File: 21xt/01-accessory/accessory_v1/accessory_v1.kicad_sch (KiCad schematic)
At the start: 31 parts, among them IC1 LT6658AHMSE-2.5#PBF, IC2 LT6658AHMSE-5#PBF, IC3 REF5025AIDR, IC7 REF5050IDR, J1 Conn_01x04

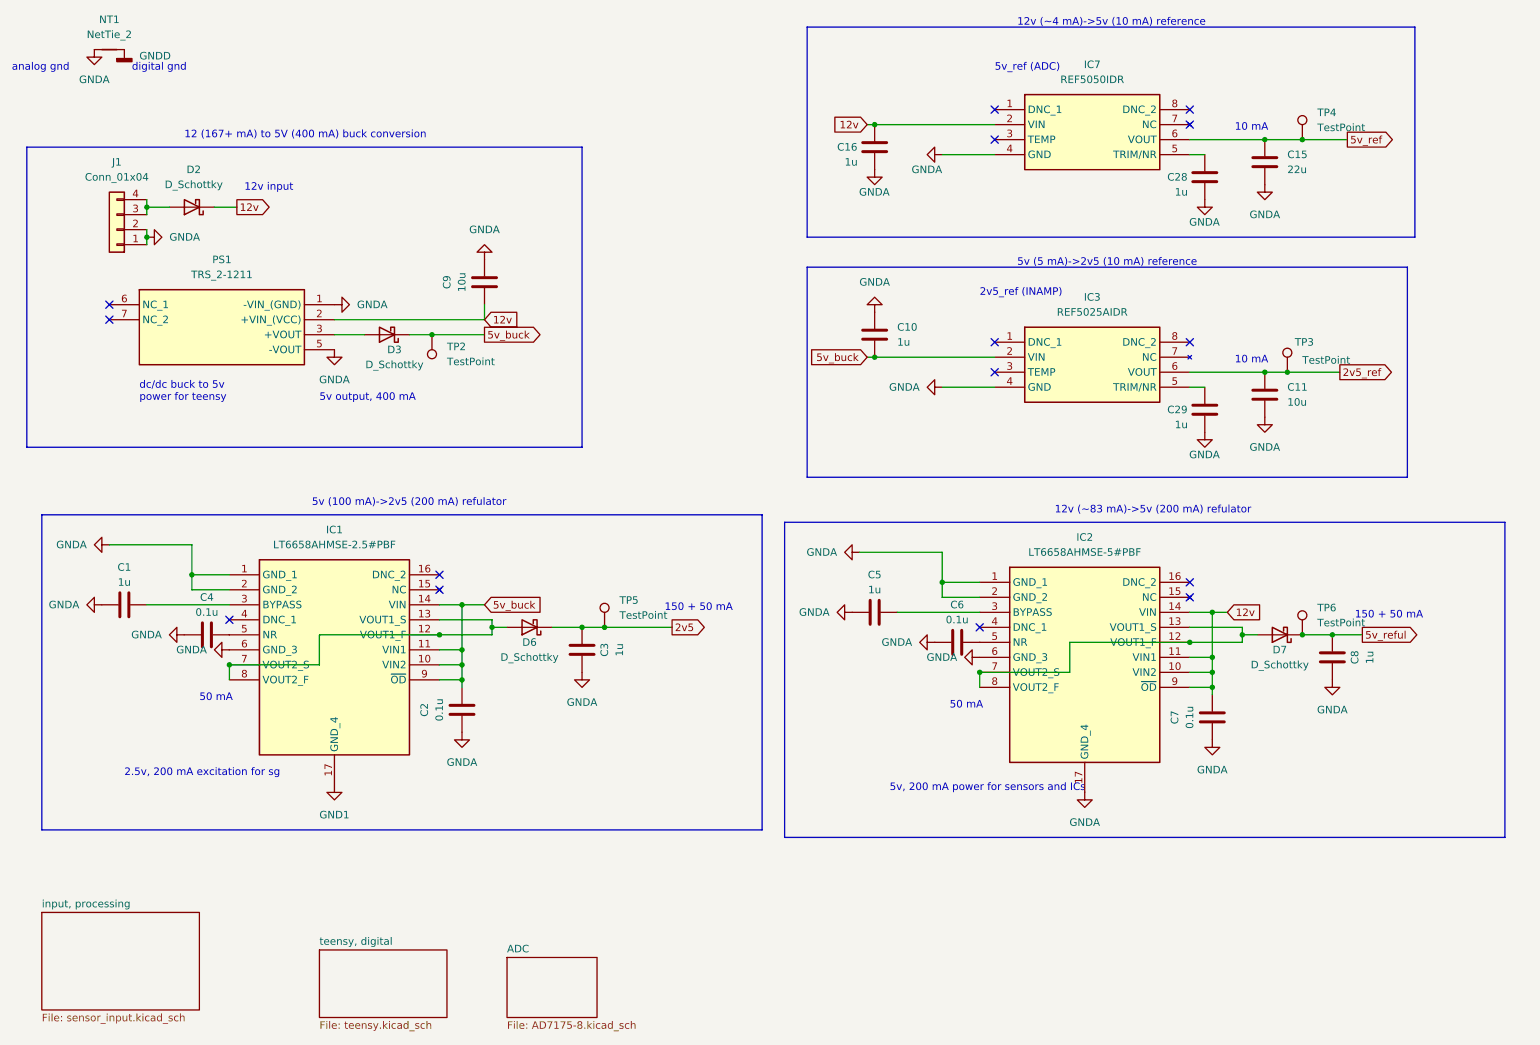
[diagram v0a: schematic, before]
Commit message: Added all accessory Rev1 3d models, added 3d models to 3d model folder and updated footprints
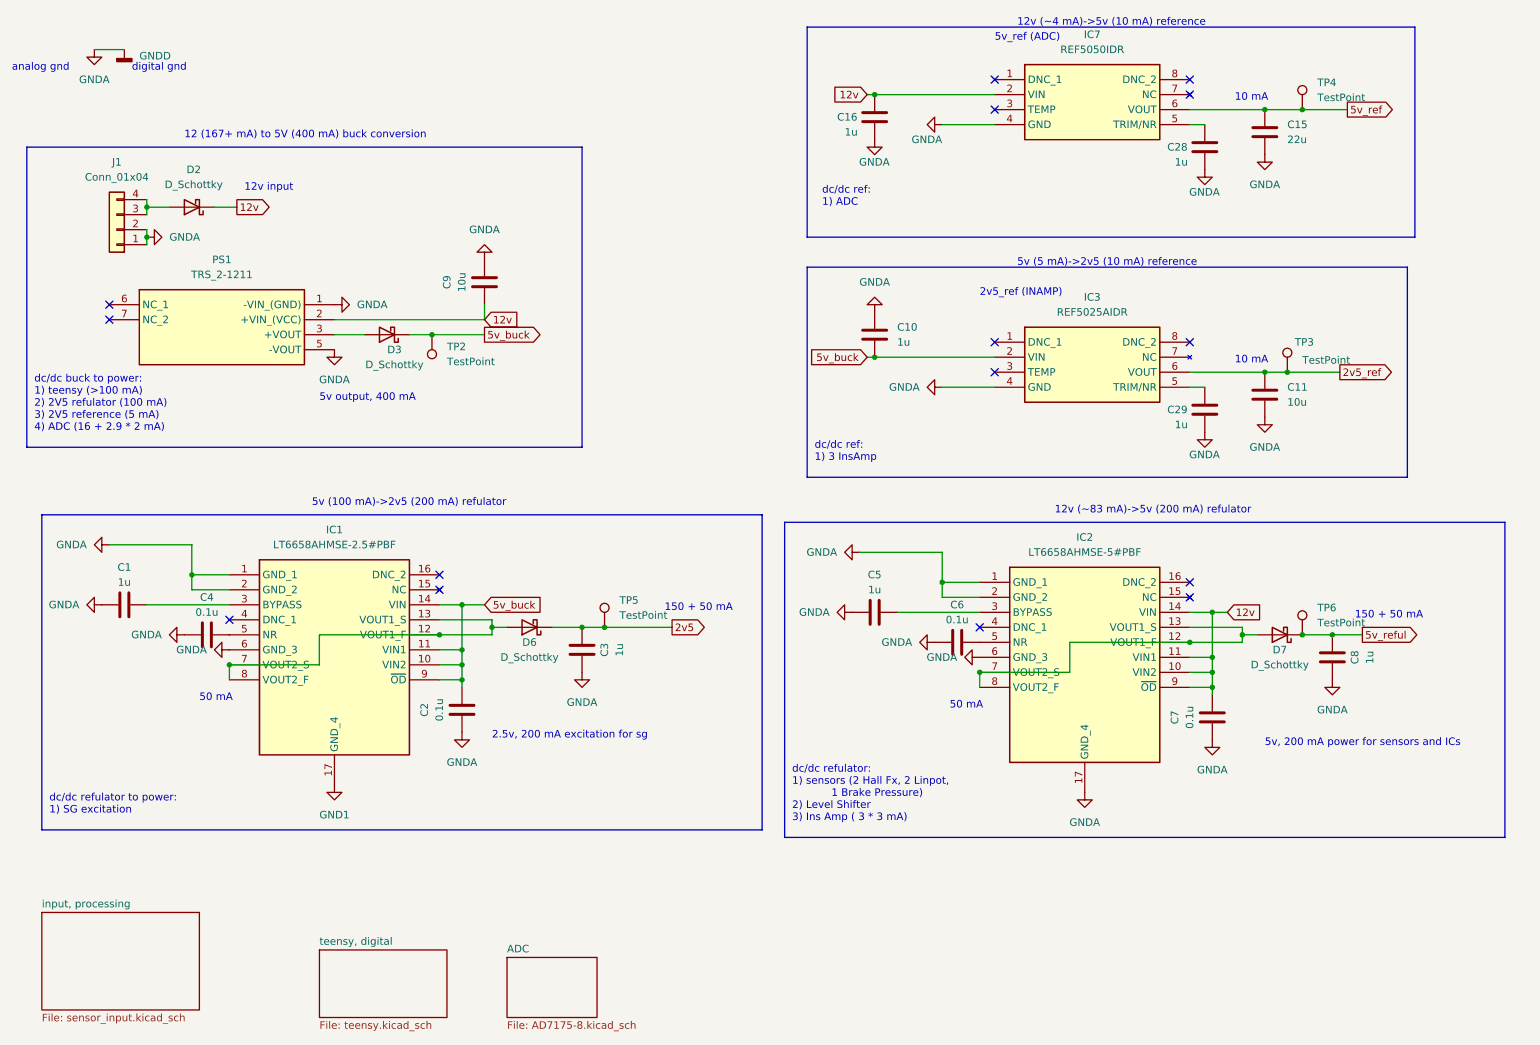
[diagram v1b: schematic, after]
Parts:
- removed NT1: NetTie_2, symbol Device:NetTie_2
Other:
- note added: "dc/dc buck to power: 1) teensy (>100 mA) 2) 2V5 refulator (100 mA) 3) 2V5 reference (5 mA) 4) ADC (16 + 2.9 * 2 mA)"
- note added: "dc/dc ref: 1) 3 InsAmp"
- note added: "dc/dc ref: 1) ADC"
- note added: "dc/dc refulator to power: 1) SG excitation"
- note added: "dc/dc refulator: 1) sensors (2 Hall Fx, 2 Linpot, 1 Brake Pressure) 2) Level Shifter 3) Ins Amp ( 3 * 3 mA)"
- note removed: "dc/dc buck to 5v power for teensy"
- moved on the sheet: C15, C16, C28, IC7, TP4

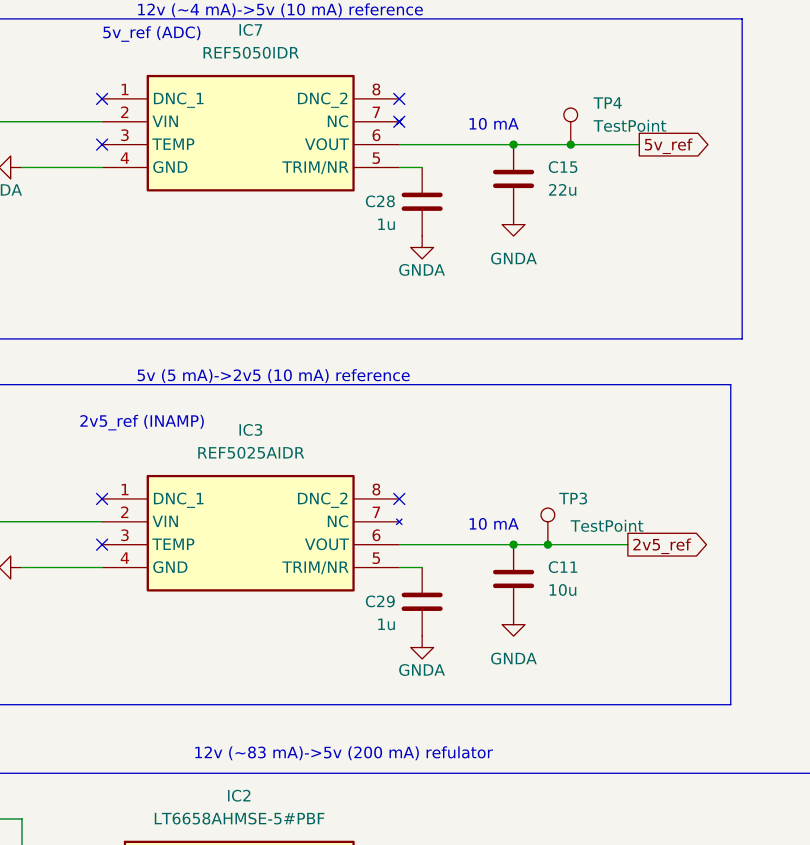
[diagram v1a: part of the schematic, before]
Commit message: Accessory V2 schematic almost done, only missing TVS diodes and checking
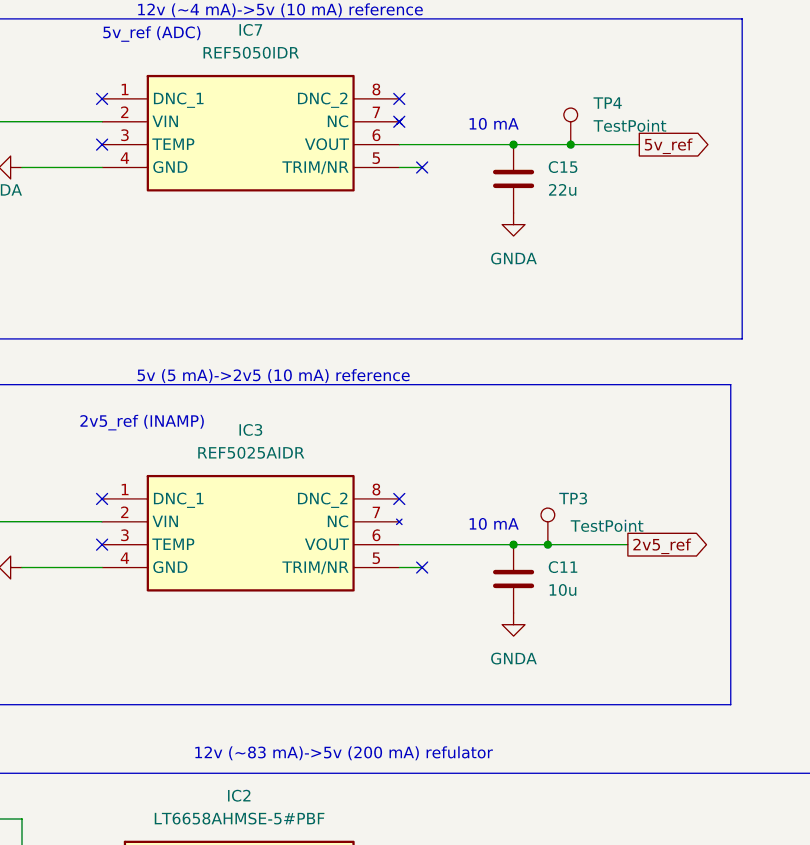
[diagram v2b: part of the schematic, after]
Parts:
- removed C28, C29: 1u, Capacitor_SMD:C_0603_1608Metric, symbol Device:C
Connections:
- no-connect marks 15 -> 17
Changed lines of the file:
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@@
   (no_connect (at 184.15 76.2))
   (no_connect (at 184.15 26.67))
+  (no_connect (at 219.71 78.74))
   (no_connect (at 217.17 29.21))
   (no_connect (at 34.29 64.77))
   (no_connect (at 217.17 71.12))
   (no_connect (at 90.17 110.49))
+  (no_connect (at 219.71 34.29))
   (no_connect (at 217.17 26.67))
   (no_connect (at 217.17 114.3))
@@
     )
   )
-  (symbol (lib_id "power:GNDA") (at 219.71 86.36 0) (unit 1)
-    (in_bom yes) (on_board yes) (dnp no)
-    (property "Reference" "#PWR064" (at 219.71 92.71 0)
-      (effects (font (size 1.27 1.27)) hide)
-    )
-    (property "Value" "GNDA" (at 222.25 90.17 0)
-      (effects (font (size 1.27 1.27)) (justify right))
-    )
-    (property "Footprint" "" (at 219.71 86.36 0)
-      (effects (font (size 1.27 1.27)) hide)
-    )
-    (property "Datasheet" "" (at 219.71 86.36 0)
-      (effects (font (size 1.27 1.27)) hide)
-    )
-    (pin "1")
-    (instances
-      (project "accessory_v1"
-        (path "/5dacc41e-ffff-47d3-9300-200c6018c603"
-          (reference "#PWR064") (unit 1)
-        )
-      )
-    )
-  )
   (symbol (lib_id "power:GNDA") (at 114.3 127 0) (unit 1)
     (in_bom yes) (on_board yes) (dnp no) (fields_autoplaced)
@@
     )
   )
-  (symbol (lib_id "power:GNDA") (at 219.71 41.91 0) (unit 1)
-    (in_bom yes) (on_board yes) (dnp no)
-    (property "Reference" "#PWR063" (at 219.71 48.26 0)
-      (effects (font (size 1.27 1.27)) hide)
-    )
-    (property "Value" "GNDA" (at 222.25 45.72 0)
-      (effects (font (size 1.27 1.27)) (justify right))
-    )
-    (property "Footprint" "" (at 219.71 41.91 0)
-      (effects (font (size 1.27 1.27)) hide)
-    )
-    (property "Datasheet" "" (at 219.71 41.91 0)
-      (effects (font (size 1.27 1.27)) hide)
-    )
-    (pin "1")
-    (instances
-      (project "accessory_v1"
-        (path "/5dacc41e-ffff-47d3-9300-200c6018c603"
-          (reference "#PWR063") (unit 1)
-        )
-      )
-    )
-  )
   (symbol (lib_id "power:GNDA") (at 220.98 138.43 0) (unit 1)
     (in_bom yes) (on_board yes) (dnp no) (fields_autoplaced)
@@
         )
       )
-    )
-  )
-  (symbol (lib_id "Device:C") (at 219.71 82.55 0) (unit 1)
-    (in_bom yes) (on_board yes) (dnp no)
-    (property "Reference" "C29" (at 213.36 82.55 0)
-      (effects (font (size 1.27 1.27)) (justify left))
-    )
-    (property "Value" "1u" (at 214.63 85.09 0)
-      (effects (font (size 1.27 1.27)) (justify left))
-    )
-    (property "Footprint" "Capacitor_SMD:C_0603_1608Metric" (at 220.6752 86.36 0)
-      (effects (font (size 1.27 1.27)) hide)
-    )
-    (property "Datasheet" "~" (at 219.71 82.55 0)
-      (effects (font (size 1.27 1.27)) hide)
-    )
-    (pin "2")
-    (pin "1")
-    (instances
-      (project "accessory_v1"
-        (path "/5dacc41e-ffff-47d3-9300-200c6018c603"
-          (reference "C29") (unit 1)
-        )
-      )
-    )
-  )
-  (symbol (lib_id "Device:C") (at 219.71 38.1 0) (unit 1)
-    (in_bom yes) (on_board yes) (dnp no)
-    (property "Reference" "C28" (at 213.36 38.1 0)
-      (effects (font (size 1.27 1.27)) (justify left))
-    )
-    (property "Value" "1u" (at 214.63 40.64 0)
-      (effects (font (size 1.27 1.27)) (justify left))
-    )
-    (property "Footprint" "Capacitor_SMD:C_0603_1608Metric" (at 220.6752 41.91 0)
-      (effects (font (size 1.27 1.27)) hide)
-    )
-    (property "Datasheet" "~" (at 219.71 38.1 0)
-      (effects (font (size 1.27 1.27)) hide)
-    )
-    (pin "2")
-    (pin "1")
-    (instances
-      (project "accessory_v1"
-        (path "/5dacc41e-ffff-47d3-9300-200c6018c603"
-          (reference "C28") (unit 1)
-        )
-      )
